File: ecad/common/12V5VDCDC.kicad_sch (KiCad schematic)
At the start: 11 parts, among them U4 MIC4680YM

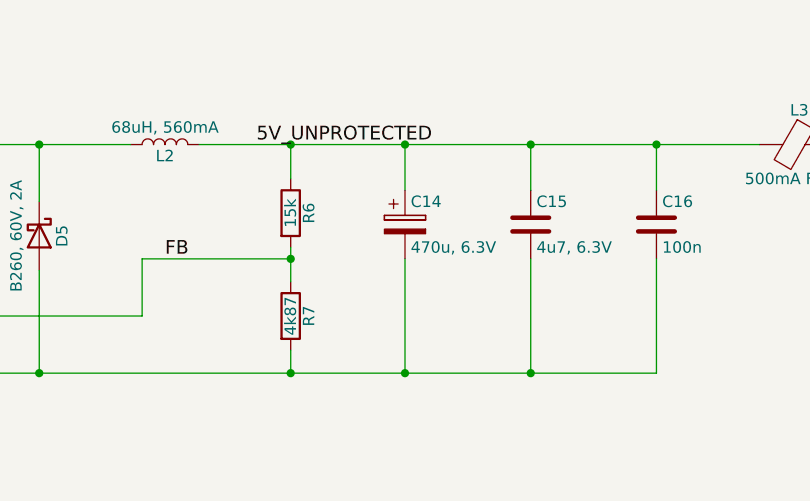
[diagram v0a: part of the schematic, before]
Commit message: Updates Arke to new Connector
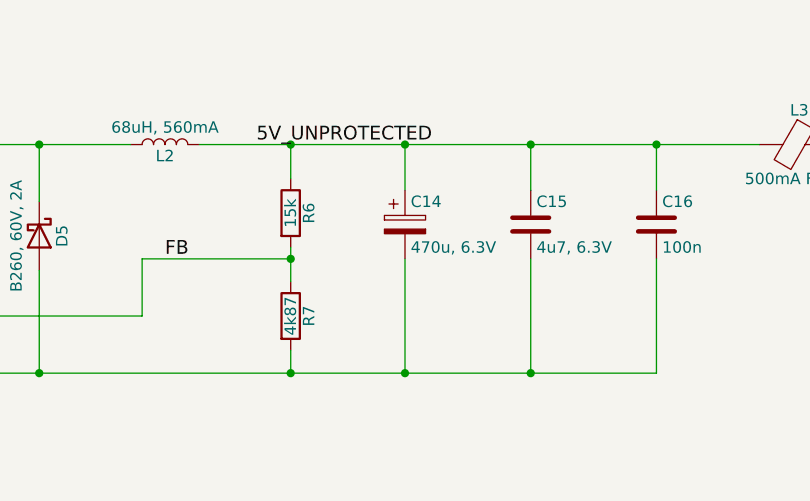
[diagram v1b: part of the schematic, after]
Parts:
- C13: MPN CL31A226KAHNNNE -> (none)
- C14: symbol celaeno-rescue:CP-Device -> Device:C_Polarized
- C16: MPN GPC0603104 -> (none)
- L1, L3: symbol celaeno-rescue:Ferrite_Bead-Device -> Device:FerriteBead

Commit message: Updates Zeus BOM
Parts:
- C13: MPN (none) -> CL31A226KAHNNNE
- C14: MPN (none) -> T491D477K006AT
- C15: MPN (none) -> GPC0603475-10
- C16: MPN (none) -> GRPC0603104
- D5: MPN (none) -> B260-13-F
- L1, L3: MPN (none) -> BLM18AG471SN1D
- L2: MPN (none) -> 744773168
- R6: MPN (none) -> GPR060315K
- R7: MPN (none) -> CRCW06034K87FKEA
- U4: MPN (none) -> MIC4680-5.0YM
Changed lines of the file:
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@@
+			)
+		)
+		(property "MPN" "MIC4680-5.0YM"
+			(at 130.81 92.71 0)
+			(effects
+				(font
+					(size 1.27 1.27)
+				)
+				(hide yes)
 			)
 		)
@@
 			)
 		)
+		(property "MPN" "B260-13-F"
+			(at 156.21 97.79 0)
+			(effects
+				(font
+					(size 1.27 1.27)
+				)
+				(hide yes)
+			)
+		)
 		(pin "1"
 		)
@@
 			)
 		)
+		(property "MPN" "744773168"
+			(at 170.18 87.63 0)
+			(effects
+				(font
+					(size 1.27 1.27)
+				)
+				(hide yes)
+			)
+		)
 		(pin "1"
 		)
@@
 			)
 		)
+		(property "MPN" "GPR060315K"
+			(at 184.15 95.25 0)
+			(effects
+				(font
+					(size 1.27 1.27)
+				)
+				(hide yes)
+			)
+		)
 		(pin "1"
 		)
@@
 			)
 		)
+		(property "MPN" "CRCW06034K87FKEA"
+			(at 184.15 106.68 0)
+			(effects
+				(font
+					(size 1.27 1.27)
+				)
+				(hide yes)
+			)
+		)
 		(pin "1"
 		)
@@
 			)
 		)
+		(property "MPN" "T491D477K006AT"
+			(at 196.85 96.52 0)
+			(effects
+				(font
+					(size 1.27 1.27)
+				)
+				(hide yes)
+			)
+		)
 		(pin "1"
 		)
@@
 			)
 		)
-		(property "Datasheet" ""
+		(property "Datasheet" "~"
 			(at 210.82 96.52 0)
 			(effects
@@
 			)
 		)
+		(property "MPN" "GPC0603475-10"
+			(at 210.82 96.52 0)
+			(effects
+				(font
+					(size 1.27 1.27)
+				)
+				(hide yes)
+			)
+		)
 		(pin "1"
 		)
@@
 			)
 		)
-		(property "Datasheet" ""
+		(property "Datasheet" "~"
 			(at 224.79 96.52 0)
 			(effects
@@
 			)
 		)
+		(property "MPN" "GRPC0603104"
+			(at 224.79 96.52 0)
+			(effects
+				(font
+					(size 1.27 1.27)
+				)
+				(hide yes)
+			)
+		)
 		(pin "1"
 		)
@@
 			)
 		)
-		(property "Datasheet" ""
+		(property "Datasheet" "~"
 			(at 97.79 95.25 0)
 			(effects
@@
 			)
 		)
+		(property "MPN" "CL31A226KAHNNNE"
+			(at 97.79 95.25 0)
+			(effects
+				(font
+					(size 1.27 1.27)
+				)
+				(hide yes)
+			)
+		)
 		(pin "1"
 		)
@@
 			)
 		)
+		(property "MPN" "BLM18AG471SN1D"
+			(at 240.03 87.63 0)
+			(effects
+				(font
+					(size 1.27 1.27)
+				)
+				(hide yes)
+			)
+		)
 		(pin "2"
 		)
@@
 			(at 83.82 87.63 0)
 			(effects
+				(font
+					(size 1.27 1.27)
+				)
+				(hide yes)
+			)
+		)
+		(property "MPN" "BLM18AG471SN1D"
+			(at 83.82 87.63 0)
+			(effects

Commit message: Polishes production of Zeus
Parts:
- C16: MPN GRPC0603104 -> GPC0603104
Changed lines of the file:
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@@
 			)
 		)
-		(property "MPN" "GRPC0603104"
+		(property "MPN" "GPC0603104"
 			(at 224.79 96.52 0)
 			(effects

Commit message: Fixes layout after receiving PCBs
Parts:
- L2: footprint Inductor_SMD:L_Wuerth_WE-PD2-Typ-MS -> FORT:L_Wuerth_WE-PD2
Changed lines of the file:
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@@
 			)
 		)
-		(property "Footprint" "Inductor_SMD:L_Wuerth_WE-PD2-Typ-MS"
+		(property "Footprint" "FORT:L_Wuerth_WE-PD2"
 			(at 170.18 87.63 0)
 			(effects
